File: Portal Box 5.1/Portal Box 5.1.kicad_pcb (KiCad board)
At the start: 2 copper layers, 120 x 80 mm, 80 parts, among them J1 Conn_01x04, J2 Conn_01x04, J3 Conn_01x02, J4 732-6001-1-ND, J5 RFID-RC522, J6 609-87520-0010ALFCT-ND, J7 2073-USB4105-GF-ACT-ND, J8 A 14-LC-TT, K1 PR28-5V-360-1A-E, Q1 NTR5103NT1G, Q2 NTR5103NT1G, SW1 141-TL3336AF160QCT-ND, U1 448-TLE4971A050T5UE0001XUMA1C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, U2 497-5026-1-ND, U3 ESP32-S3-DEVKITC-1-N8R8-OFFIC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, U4 497-5026-1-ND, U5 AP7363-33D-13

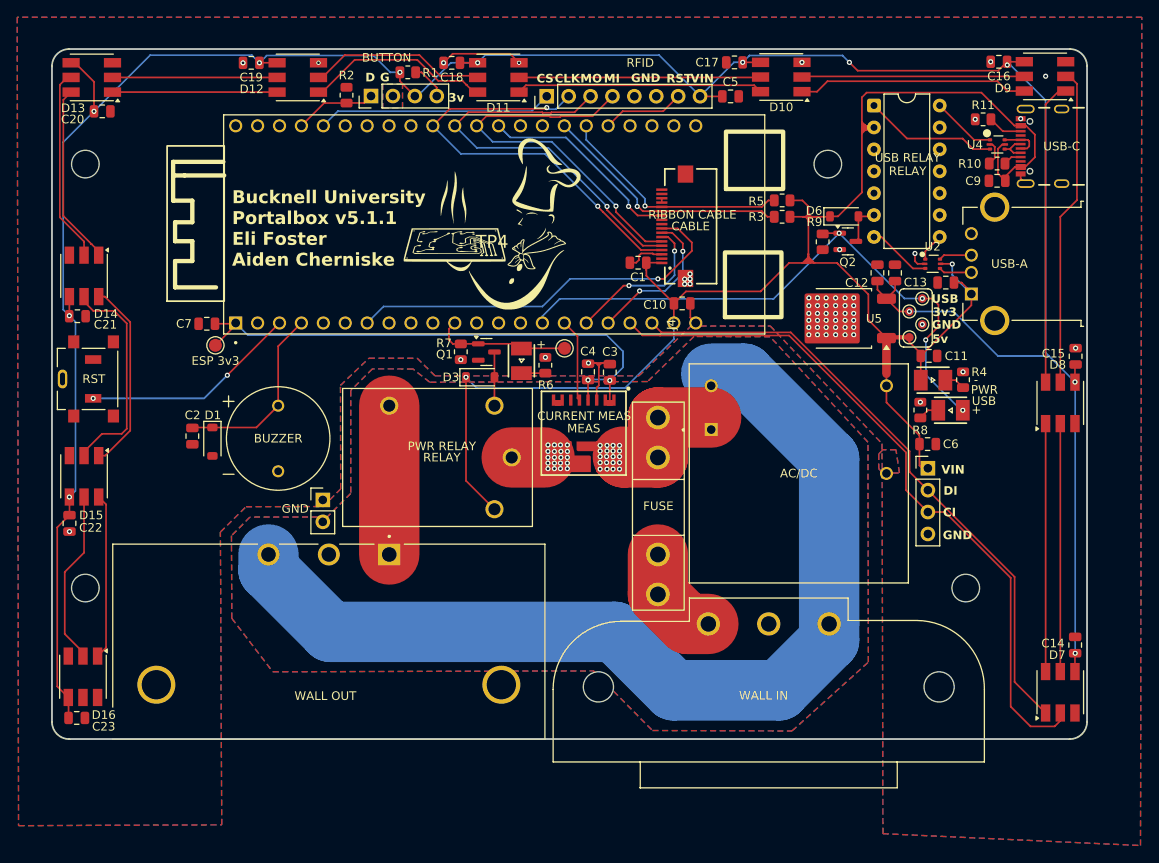
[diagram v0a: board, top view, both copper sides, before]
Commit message: chore: fix labels, solid pad connections, and version no.
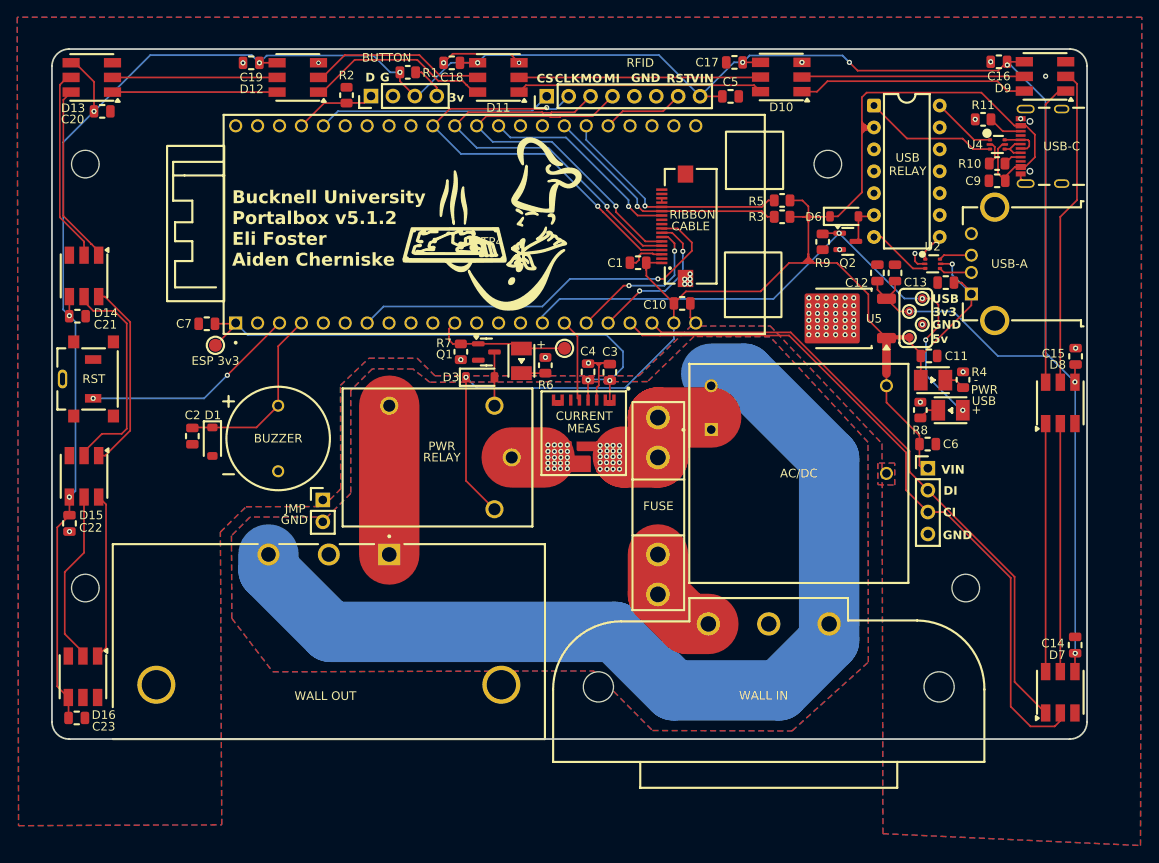
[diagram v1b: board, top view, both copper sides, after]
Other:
- board text added: "Bucknell University Portalbox v5.1.2 Eli Foster Aiden Cherniske"
- board text removed: "Bucknell University Portalbox v5.1.1 Eli Foster Aiden Cherniske"

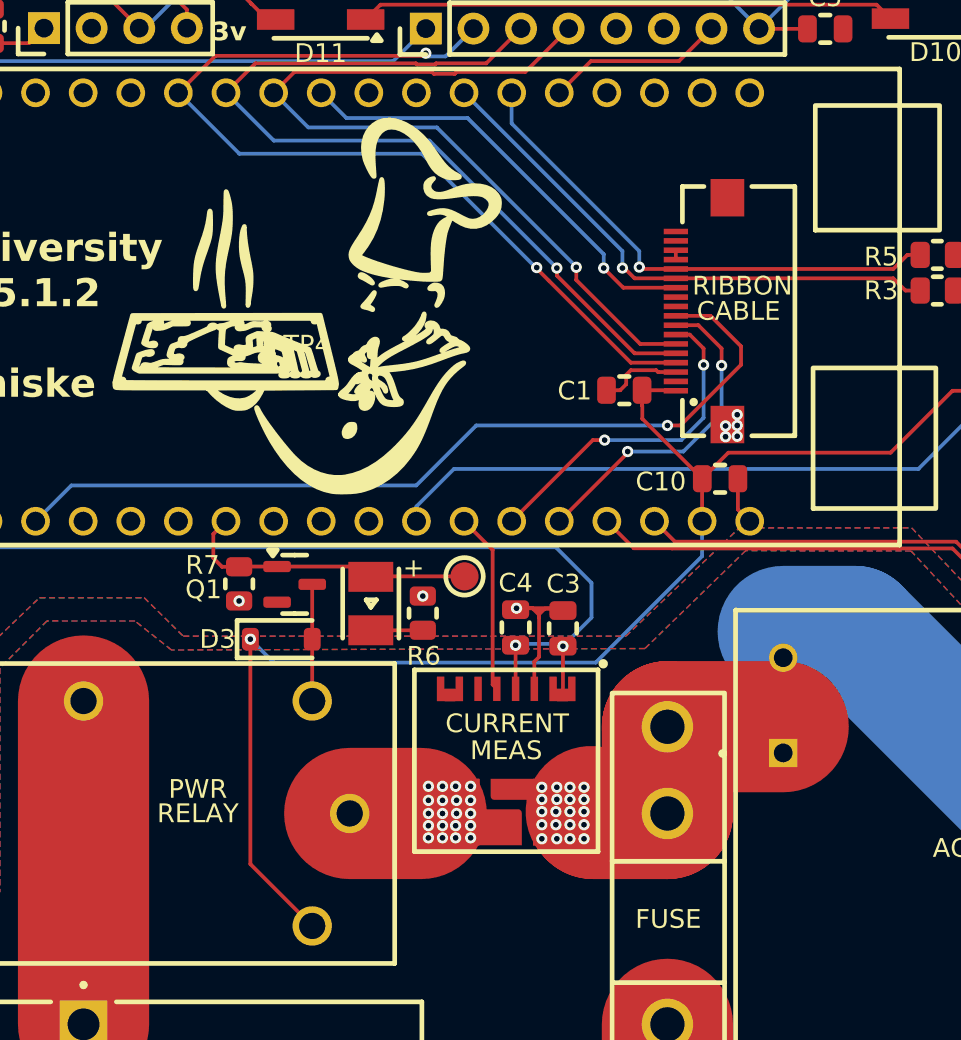
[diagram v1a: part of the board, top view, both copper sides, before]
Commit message: fix drc errors and remove tp4 reference
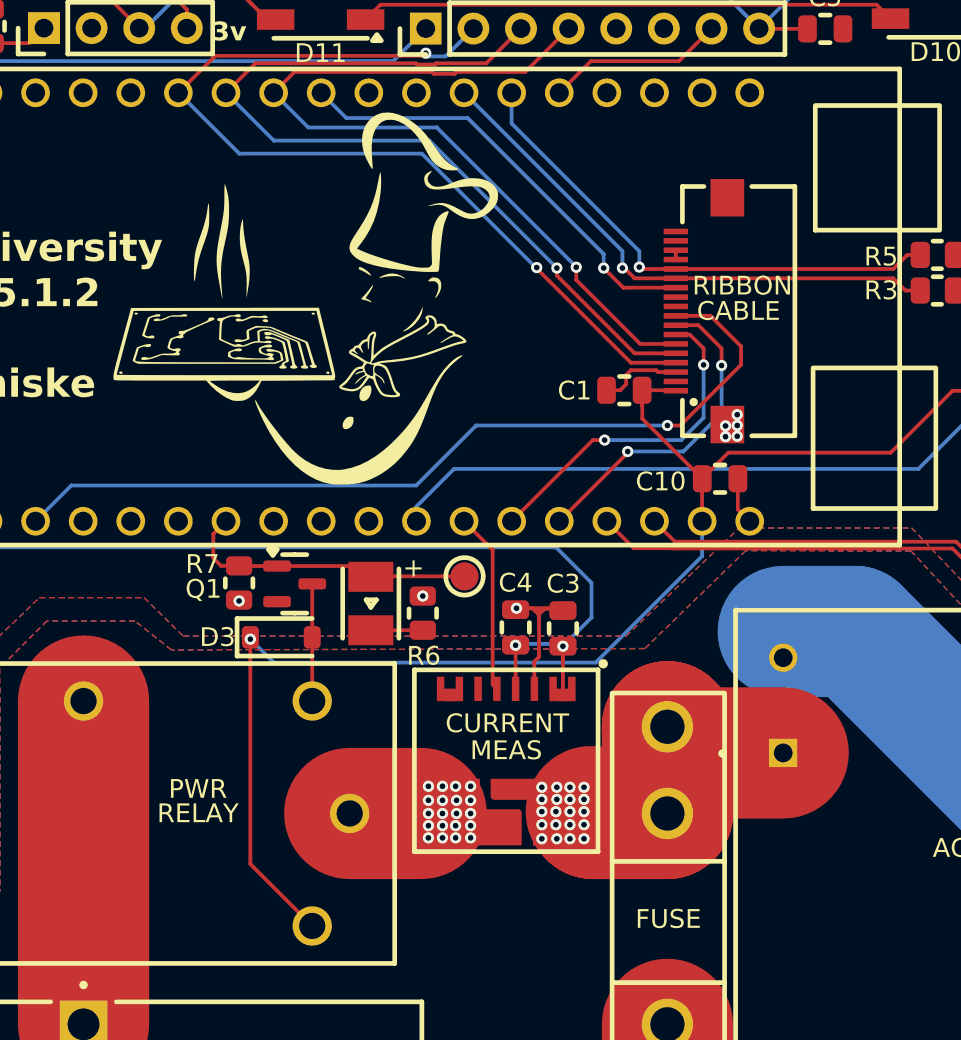
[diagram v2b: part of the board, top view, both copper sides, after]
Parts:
- removed TP4: Silkscreen Image, portalbox:MakerELogoSilkscreen
- added G***: LOGO, portalbox:MakerELogoSilkscreen, F.Cu at (139.9, 75.1)
- moved D3 0.10 mm to (138.6, 91.1)
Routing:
- net /WALL_HOT_FUSED: track 14.9 -> 15.5 mm
